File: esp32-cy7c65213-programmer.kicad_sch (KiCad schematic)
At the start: 25 parts, among them J1 USB_C, J2 Conn_01x07, Q1 2N3904, Q2 2N3904, U1 TLV1117-33, U2 CY7C65213-28PVXI

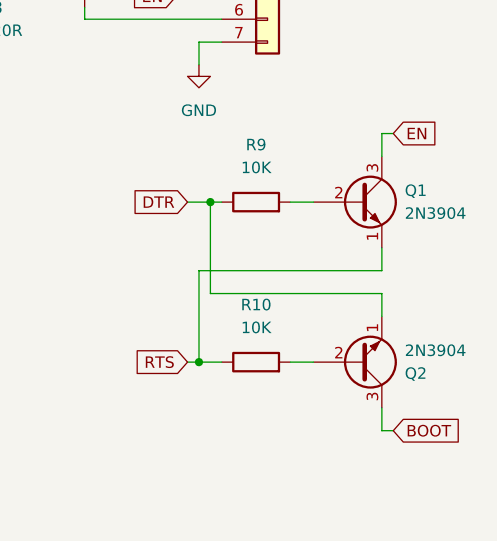
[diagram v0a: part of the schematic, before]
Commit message: Fix wrong transistor type and update the screenshots
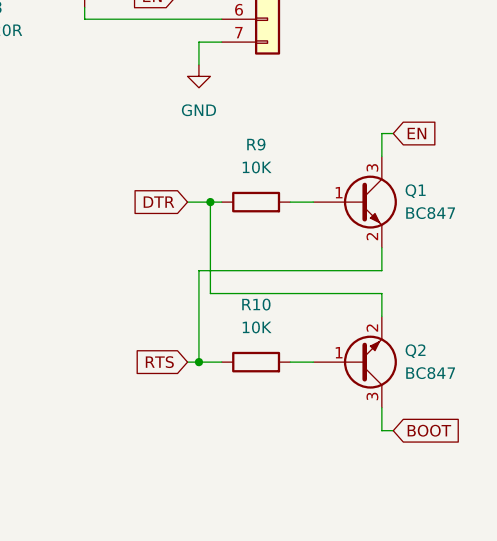
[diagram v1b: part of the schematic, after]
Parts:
- removed Q1, Q2: 2N3904, Package_TO_SOT_SMD:SOT-23_Handsoldering, symbol Transistor_BJT:2N3904
- added Q1, Q2: BC847, Package_TO_SOT_SMD:SOT-23_Handsoldering, symbol Transistor_BJT:BC847
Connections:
- net BOOT: now also Q2.3 (C)
- net DTR: now also Q2.2 (E)
- net EN: now also Q1.3 (C)
- net RTS: now also Q1.2 (E)
- net at R9.2: now also Q1.1 (B)
- net at R10.2: now also Q2.1 (B)
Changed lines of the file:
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@@
     (pin "1")
-  )
-  (symbol (lib_id "Transistor_BJT:2N3904") (at 250.19 101.6 0) (mirror x) (unit 1)
-    (in_bom yes) (on_board yes) (fields_autoplaced)
-    (property "Reference" "Q2" (id 0) (at 255.27 102.8701 0)
-      (effects (font (size 1.27 1.27)) (justify left))
-    )
-    (property "Value" "2N3904" (id 1) (at 255.27 100.3301 0)
-      (effects (font (size 1.27 1.27)) (justify left))
-    )
-    (property "Footprint" "Package_TO_SOT_SMD:SOT-23_Handsoldering" (id 2) (at 255.27 99.695 0)
-      (effects (font (size 1.27 1.27) italic) (justify left) hide)
-    )
-    (property "Datasheet" "https://www.onsemi.com/pub/Collateral/2N3903-D.PDF" (id 3) (at 250.19 101.6 0)
-      (effects (font (size 1.27 1.27)) (justify left) hide)
-    )
-    (pin "1")
-    (pin "2")
-    (pin "3")
   )
   (symbol (lib_id "power:+3.3V") (at 205.74 46.99 0) (unit 1)
@@
     (pin "9")
   )
-  (symbol (lib_id "Transistor_BJT:2N3904") (at 250.19 83.82 0) (unit 1)
-    (in_bom yes) (on_board yes) (fields_autoplaced)
-    (property "Reference" "Q1" (id 0) (at 255.27 82.5499 0)
-      (effects (font (size 1.27 1.27)) (justify left))
-    )
-    (property "Value" "2N3904" (id 1) (at 255.27 85.0899 0)
-      (effects (font (size 1.27 1.27)) (justify left))
-    )
-    (property "Footprint" "Package_TO_SOT_SMD:SOT-23_Handsoldering" (id 2) (at 255.27 85.725 0)
-      (effects (font (size 1.27 1.27) italic) (justify left) hide)
-    )
-    (property "Datasheet" "https://www.onsemi.com/pub/Collateral/2N3903-D.PDF" (id 3) (at 250.19 83.82 0)
-      (effects (font (size 1.27 1.27)) (justify left) hide)
-    )
-    (pin "1")
-    (pin "2")
-    (pin "3")
-  )
   (symbol (lib_id "Device:C") (at 76.2 96.52 0) (unit 1)
     (in_bom yes) (on_board yes)
@@
     (pin "2")
   )
+  (symbol (lib_id "Transistor_BJT:BC847") (at 250.19 83.82 0) (unit 1)
+    (in_bom yes) (on_board yes) (fields_autoplaced)
+    (property "Reference" "Q1" (id 0) (at 255.27 82.5499 0)
+      (effects (font (size 1.27 1.27)) (justify left))
+    )
+    (property "Value" "BC847" (id 1) (at 255.27 85.0899 0)
+      (effects (font (size 1.27 1.27)) (justify left))
+    )
+    (property "Footprint" "Package_TO_SOT_SMD:SOT-23_Handsoldering" (id 2) (at 255.27 85.725 0)
+      (effects (font (size 1.27 1.27) italic) (justify left) hide)
+    )
+    (property "Datasheet" "http://www.infineon.com/dgdl/Infineon-BC847SERIES_BC848SERIES_BC849SERIES_BC850SERIES-DS-v01_01-en.pdf?fileId=db3a304314dca389011541d4630a1657" (id 3) (at 250.19 83.82 0)
+      (effects (font (size 1.27 1.27)) (justify left) hide)
+    )
+    (pin "1")
+    (pin "2")
+    (pin "3")
+  )
   (symbol (lib_id "Regulator_Linear:TLV1117-33") (at 110.49 55.88 0) (unit 1)
     (in_bom yes) (on_board yes) (fields_autoplaced)
@@
     (pin "1")
     (pin "2")
+  )
+  (symbol (lib_id "Transistor_BJT:BC847") (at 250.19 101.6 0) (mirror x) (unit 1)
+    (in_bom yes) (on_board yes) (fields_autoplaced)
+    (property "Reference" "Q2" (id 0) (at 255.27 100.3299 0)
+      (effects (font (size 1.27 1.27)) (justify left))
+    )
+    (property "Value" "BC847" (id 1) (at 255.27 102.8699 0)
+      (effects (font (size 1.27 1.27)) (justify left))
+    )
+    (property "Footprint" "Package_TO_SOT_SMD:SOT-23_Handsoldering" (id 2) (at 255.27 99.695 0)
+      (effects (font (size 1.27 1.27) italic) (justify left) hide)
+    )
+    (property "Datasheet" "http://www.infineon.com/dgdl/Infineon-BC847SERIES_BC848SERIES_BC849SERIES_BC850SERIES-DS-v01_01-en.pdf?fileId=db3a304314dca389011541d4630a1657" (id 3) (at 250.19 101.6 0)
+      (effects (font (size 1.27 1.27)) (justify left) hide)
+    )
+    (pin "1")
+    (pin "2")
+    (pin "3")
   )
   (symbol (lib_id "Device:LED") (at 200.66 90.17 0) (unit 1)
@@
       (reference "J2") (unit 1) (value "Conn_01x07") (footprint "Connector_PinHeader_2.54mm:PinHeader_1x07_P2.54mm_Horizontal")
     )
-    (path "/227753ce-dc05-4f8e-bf0d-fe1485d98829"
-      (reference "Q1") (unit 1) (value "2N3904") (footprint "Package_TO_SOT_SMD:SOT-23_Handsoldering")
-    )
-    (path "/12af6062-b91c-42a8-abae-3f5f404d2f10"
-      (reference "Q2") (unit 1) (value "2N3904") (footprint "Package_TO_SOT_SMD:SOT-23_Handsoldering")
+    (path "/4f935670-c710-4994-aacd-9741b7a986b4"
+      (reference "Q1") (unit 1) (value "BC847") (footprint "Package_TO_SOT_SMD:SOT-23_Handsoldering")
+    )
+    (path "/77660536-4348-424c-a8fe-0608ac509d83"
+      (reference "Q2") (unit 1) (value "BC847") (footprint "Package_TO_SOT_SMD:SOT-23_Handsoldering")
     )
     (path "/8316a672-8de7-4d2a-a40f-3a25b0e57957"
